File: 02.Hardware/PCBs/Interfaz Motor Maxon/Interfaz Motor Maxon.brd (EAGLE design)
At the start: 44.3 x 40.8 mm, 4 parts, among them J1 1-84953-1, J2 52207-1133

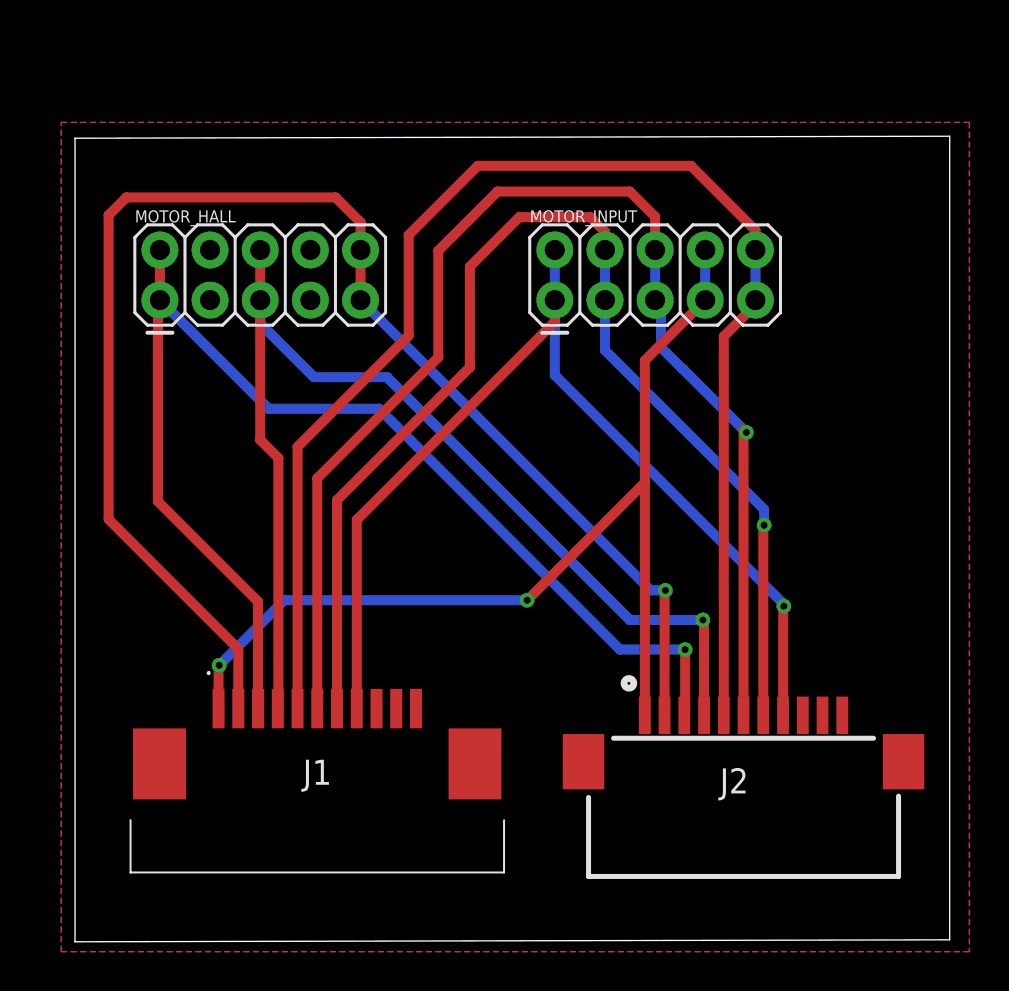
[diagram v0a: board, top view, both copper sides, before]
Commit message: añadidas vias entre planos masa top y bottom
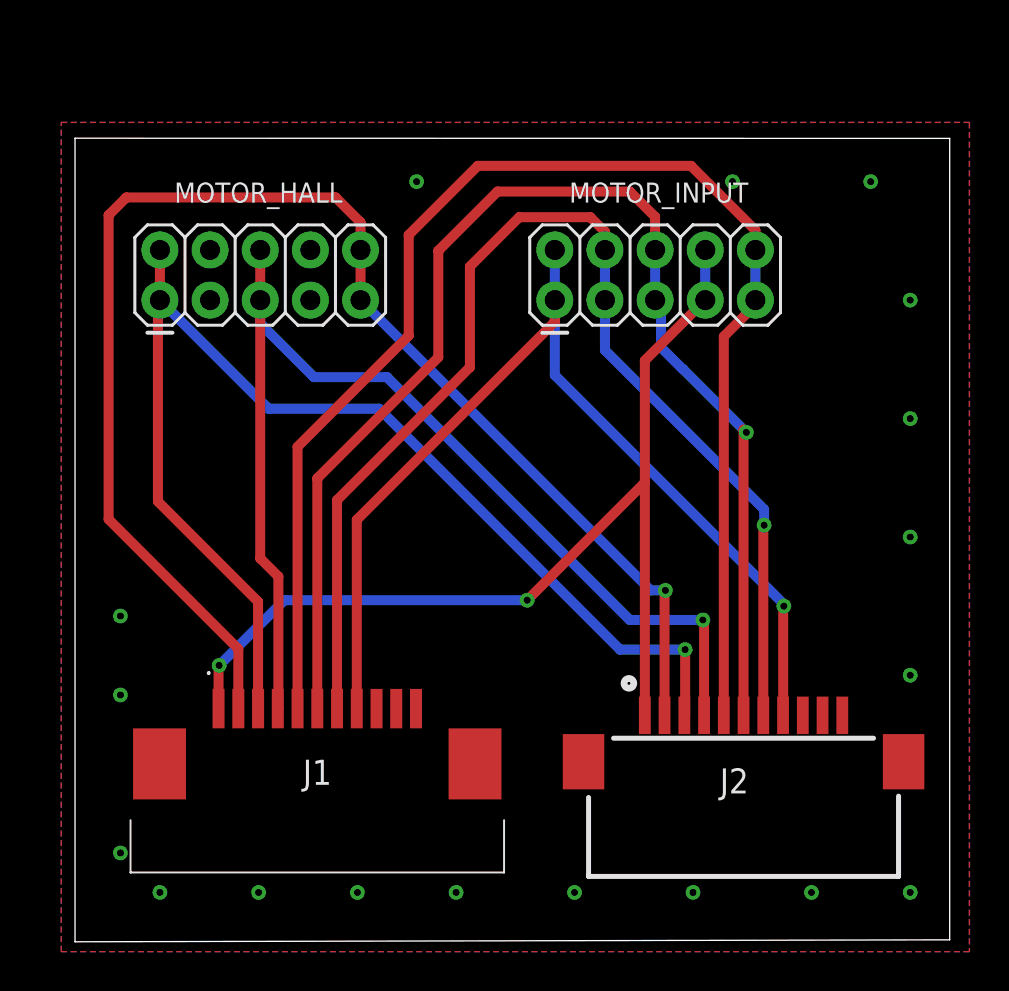
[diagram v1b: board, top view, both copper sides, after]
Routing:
- net GND: vias 0 -> 18
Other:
- board size 44.3 x 40.8 mm -> 44.3 x 40.7 mm
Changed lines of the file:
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@@
 <drawing>
 <settings>
-<setting alwaysvectorfont="no"/>
+<setting alwaysvectorfont="yes"/>
 <setting verticaltext="up"/>
 </settings>
@@
 <layer number="2" name="Route2" color="16" fill="1" visible="no" active="no"/>
 <layer number="15" name="Route15" color="23" fill="1" visible="no" active="no"/>
-<layer number="16" name="Bottom" color="1" fill="1" visible="yes" active="yes"/>
+<layer number="16" name="Bottom" color="1" fill="1" visible="no" active="yes"/>
 <layer number="17" name="Pads" color="2" fill="1" visible="yes" active="yes"/>
 <layer number="18" name="Vias" color="2" fill="1" visible="yes" active="yes"/>
@@
 <plain>
 <wire x1="1.7" y1="2.5" x2="46" y2="2.6" width="0" layer="20"/>
-<wire x1="46" y1="2.6" x2="46" y2="43.3" width="0" layer="20"/>
-<wire x1="46" y1="43.3" x2="1.7" y2="43.2" width="0" layer="20"/>
+<wire x1="46" y1="2.6" x2="46" y2="43.19" width="0" layer="20"/>
+<wire x1="46" y1="43.19" x2="1.7" y2="43.2" width="0" layer="20"/>
 <wire x1="1.7" y1="43.2" x2="1.7" y2="2.5" width="0" layer="20"/>
 <text x="42.8" y="22.9" size="1.778" layer="22" rot="MR0">Interfaz Maxon
@@
 </element>
 <element name="MOTOR_INPUT" library="SparkFun-Connectors" library_urn="urn:adsk.eagle:library:513" package="2X5" package3d_urn="urn:adsk.eagle:package:38012/1" value="" x="26" y="35" smashed="yes">
-<attribute name="NAME" x="24.73" y="38.937" size="0.6096" layer="25" font="vector" ratio="20"/>
+<attribute name="NAME" x="26.73" y="39.937" size="1.016" layer="25" font="vector" ratio="13"/>
 <attribute name="PROD_ID" value="CONN-08499" x="26" y="35" size="1.778" layer="27" display="off"/>
 <attribute name="SF_ID" value="PRT-0778" x="26" y="35" size="1.778" layer="27" display="off"/>
@@
 </element>
 <element name="MOTOR_HALL" library="SparkFun-Connectors" library_urn="urn:adsk.eagle:library:513" package="2X5" package3d_urn="urn:adsk.eagle:package:38012/1" value="" x="6" y="35" smashed="yes">
-<attribute name="NAME" x="4.73" y="38.937" size="0.6096" layer="25" font="vector" ratio="20"/>
+<attribute name="NAME" x="6.73" y="39.937" size="1.016" layer="25" font="vector" ratio="13"/>
 <attribute name="PROD_ID" value="CONN-08499" x="6" y="35" size="1.778" layer="27" display="off"/>
 <attribute name="SF_ID" value="PRT-0778" x="6" y="35" size="1.778" layer="27" display="off"/>
@@
 <contactref element="MOTOR_HALL" pad="5"/>
 <contactref element="MOTOR_HALL" pad="6"/>
-<wire x1="11.08" y1="35" x2="11.08" y2="34.7" width="0.508" layer="1"/>
-<wire x1="11.08" y1="34.7" x2="11.08" y2="27.92" width="0.508" layer="1"/>
-<wire x1="11.08" y1="27.92" x2="12" y2="27" width="0.508" layer="1"/>
-<wire x1="12" y1="27" x2="12" y2="14.34" width="0.508" layer="1"/>
+<wire x1="11.08" y1="35" x2="11.08" y2="21.92" width="0.508" layer="1"/>
+<wire x1="11.08" y1="21.92" x2="12" y2="21" width="0.508" layer="1"/>
+<wire x1="12" y1="21" x2="12" y2="14.34" width="0.508" layer="1"/>
 <wire x1="12" y1="14.34" x2="11.97" y2="14.31" width="0.508" layer="1"/>
 <wire x1="33.56" y1="13.97" x2="33.56" y2="18.74" width="0.508" layer="1"/>
@@
 <vertex x="1" y="2"/>
 </polygon>
+<via x="4" y="19" extent="1-16" drill="0.35"/>
+<via x="4" y="15" extent="1-16" drill="0.35"/>
+<via x="4" y="7" extent="1-16" drill="0.35"/>
+<via x="6" y="5" extent="1-16" drill="0.35"/>
+<via x="11" y="5" extent="1-16" drill="0.35"/>
+<via x="16" y="5" extent="1-16" drill="0.35"/>
+<via x="21" y="5" extent="1-16" drill="0.35"/>
+<via x="27" y="5" extent="1-16" drill="0.35"/>
+<via x="33" y="5" extent="1-16" drill="0.35"/>
+<via x="39" y="5" extent="1-16" drill="0.35"/>
+<via x="44" y="5" extent="1-16" drill="0.35"/>
+<via x="44" y="16" extent="1-16" drill="0.35"/>
+<via x="44" y="23" extent="1-16" drill="0.35"/>
+<via x="44" y="29" extent="1-16" drill="0.35"/>
+<via x="44" y="35" extent="1-16" drill="0.35"/>
+<via x="42" y="41" extent="1-16" drill="0.35"/>
+<via x="35" y="41" extent="1-16" drill="0.35"/>
+<via x="19" y="41" extent="1-16" drill="0.35"/>
 </signal>
 <signal name="MOTOR_C">

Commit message: Correcion errores. Interfaz Maxon v2
Correcion de conexiones entre los conectores del motores y los conectores a la placa.
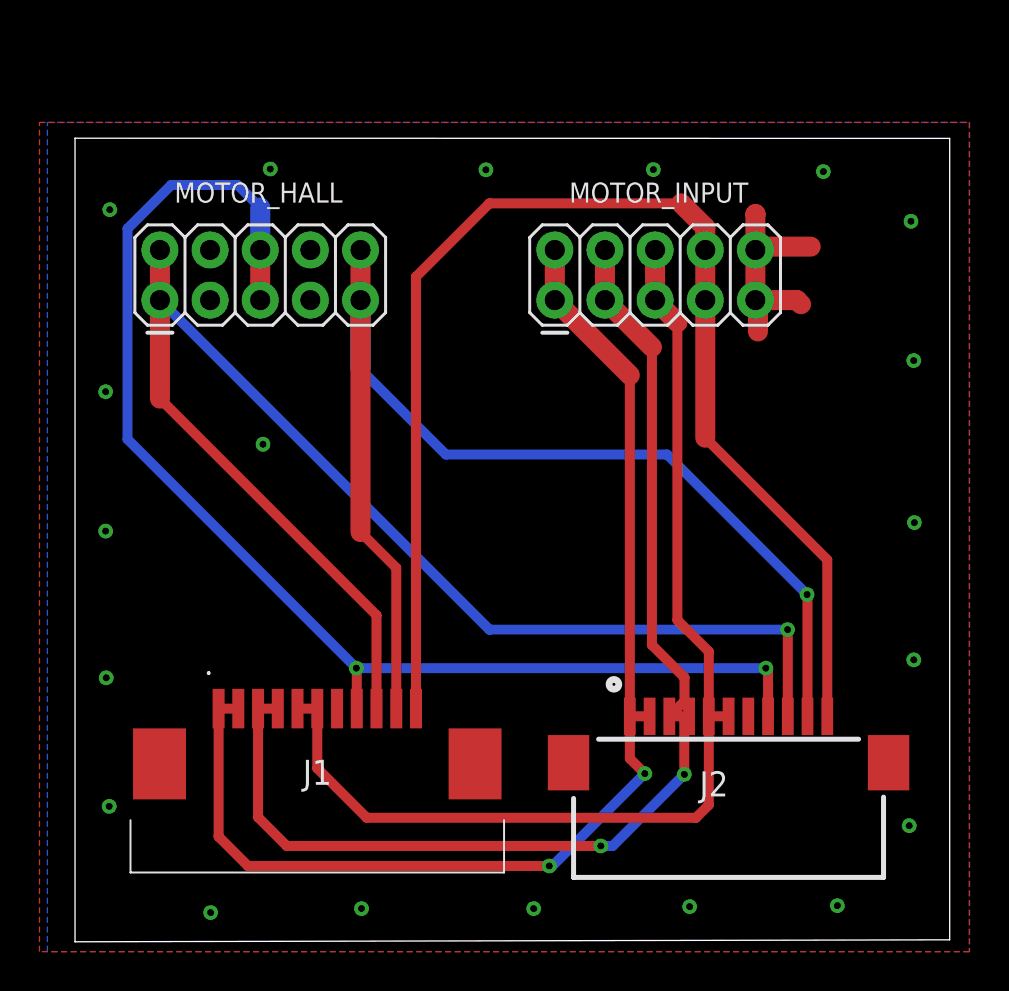
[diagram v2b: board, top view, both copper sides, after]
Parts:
- moved J2 0.76 mm to (34.8, 13.9)
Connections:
- net GND: now also J1.7, J2.7; no longer J1.5, J2.5
- net HALL_A: now also J1.9, J2.9; no longer J1.3, J2.3
- net HALL_B: now also J1.8, J2.8; no longer J1.4, J2.4
- net HALL_C: now also J1.10, J2.10; no longer J1.2, J2.2
- net MOTOR_A: now also J1.1, J1.2, J2.1, J2.2; no longer J1.8, J2.8
- net MOTOR_B: now also J1.3, J1.4, J2.3, J2.4; no longer J1.7, J2.7
- net MOTOR_C: now also J1.5, J2.5
- net VBUSBAR: now also J1.11, J2.11; no longer J1.1, J2.1
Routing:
- net GND: track 71.9 -> 11.3 mm, vias 18 -> 20
- net VBUSBAR: track 52.4 -> 65.9 mm, vias 2 -> 0
- net HALL_C: track 73.2 -> 61.0 mm
- net MOTOR_C: track 66.0 -> 55.4 mm, vias 1 -> 0
- net HALL_A: track 62.6 -> 70.9 mm
- net MOTOR_A: track 53.2 -> 61.0 mm, vias 1 -> 2
- net HALL_B: track 58.3 -> 65.1 mm, vias 1 -> 2
- net MOTOR_B: track 61.2 -> 59.9 mm, vias 1 -> 2
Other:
- board text added: "Interfaz Maxon v2-Oct22"
- board text removed: "Interfaz Maxon v1-Sep22"

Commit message: Adapatacion de la interfaz para conexión por trought hole directamente.
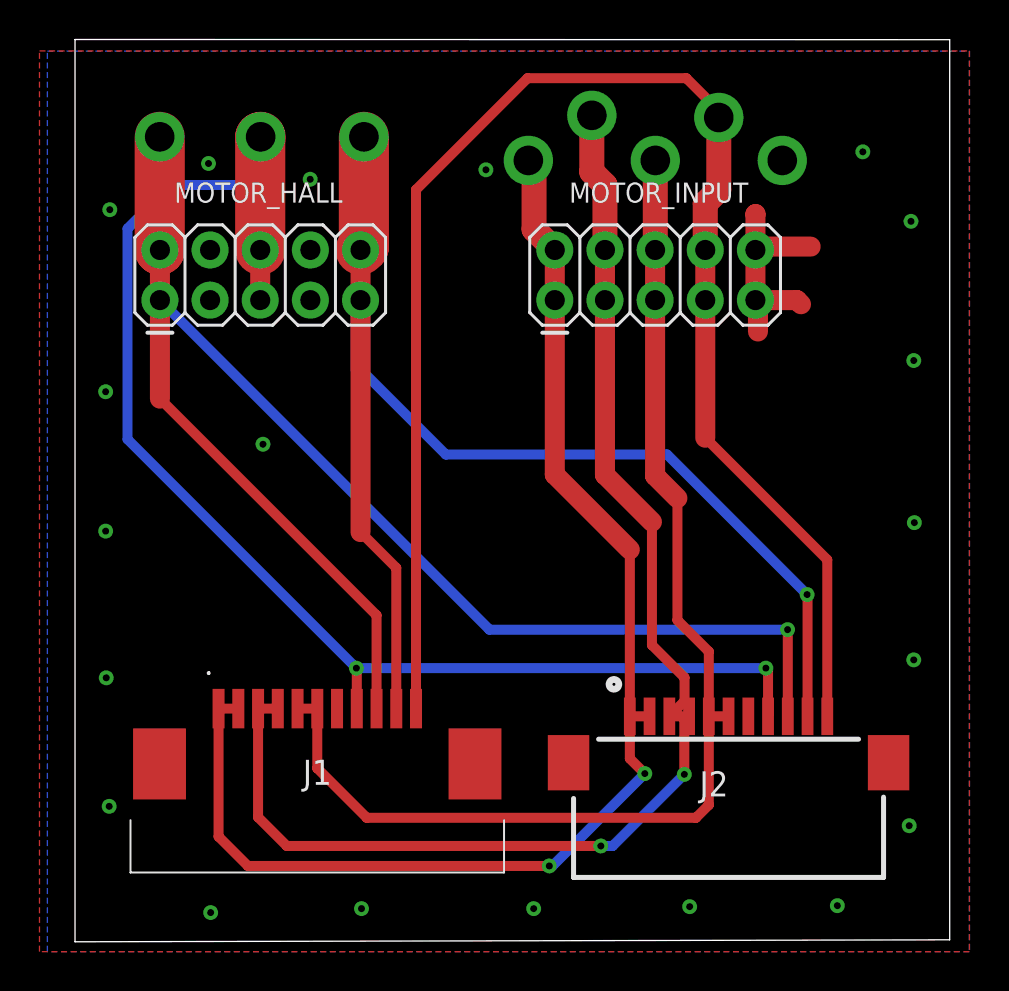
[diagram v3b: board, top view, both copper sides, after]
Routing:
- net VBUSBAR: track 65.9 -> 77.8 mm, vias 0 -> 1
- net MOTOR_B: track 59.9 -> 67.0 mm, vias 2 -> 3
- net HALL_C: track 61.0 -> 66.8 mm, vias 1 -> 2
- net HALL_B: track 65.1 -> 70.9 mm, vias 2 -> 3
- net HALL_A: track 70.9 -> 76.6 mm, vias 1 -> 2
- net MOTOR_A: track 61.0 -> 66.1 mm, vias 2 -> 3
- net MOTOR_C: track 55.4 -> 59.9 mm, vias 0 -> 1
- net GND: vias 20 -> 21
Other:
- board size 44.3 x 40.7 mm -> 44.3 x 45.7 mm
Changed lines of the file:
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@@
 <drawing>
 <settings>
-<setting alwaysvectorfont="yes"/>
+<setting alwaysvectorfont="no"/>
 <setting verticaltext="up"/>
 </settings>
@@
 <plain>
 <wire x1="1.7" y1="2.5" x2="46" y2="2.6" width="0" layer="20"/>
-<wire x1="46" y1="2.6" x2="46" y2="43.19" width="0" layer="20"/>
-<wire x1="46" y1="43.19" x2="1.7" y2="43.2" width="0" layer="20"/>
-<wire x1="1.7" y1="43.2" x2="1.7" y2="2.5" width="0" layer="20"/>
+<wire x1="46" y1="2.6" x2="46" y2="48.19" width="0" layer="20"/>
+<wire x1="46" y1="48.19" x2="1.7" y2="48.2" width="0" layer="20"/>
+<wire x1="1.7" y1="48.2" x2="1.7" y2="2.5" width="0" layer="20"/>
 <text x="42.8" y="22.9" size="1.778" layer="22" rot="MR0">Interfaz Maxon
 v2-Oct22</text>
@@
 <wire x1="20.48" y1="27.18" x2="16.16" y2="31.5" width="0.508" layer="16"/>
 <wire x1="16.16" y1="31.5" x2="16.16" y2="35" width="1.016" layer="16"/>
+<via x="16.33" y="43.27" extent="1-16" drill="1.5" diameter="2.5"/>
+<wire x1="16.33" y1="43.27" x2="16.33" y2="37.71" width="2.54" layer="1"/>
+<wire x1="16.33" y1="37.71" x2="16.16" y2="37.54" width="2.54" layer="1"/>
 </signal>
 <signal name="HALL_A">
@@
 <wire x1="37.79" y1="18.31" x2="22.69" y2="18.31" width="0.508" layer="16"/>
 <wire x1="22.69" y1="18.31" x2="6" y2="35" width="0.508" layer="16"/>
+<via x="5.99" y="43.27" extent="1-16" drill="1.5" diameter="2.5"/>
+<wire x1="5.99" y1="43.27" x2="5.99" y2="37.55" width="2.54" layer="1"/>
+<wire x1="5.99" y1="37.55" x2="6" y2="37.54" width="2.54" layer="1"/>
 </signal>
 <signal name="HALL_B">
@@
 <wire x1="9.94" y1="40.83" x2="11.08" y2="39.69" width="0.508" layer="16"/>
 <wire x1="11.08" y1="39.69" x2="11.08" y2="37.54" width="1.016" layer="16"/>
+<via x="11.1" y="43.27" extent="1-16" drill="1.5" diameter="2.5"/>
+<wire x1="11.08" y1="37.54" x2="11.08" y2="43.25" width="2.54" layer="1"/>
+<wire x1="11.08" y1="43.25" x2="11.1" y2="43.27" width="2.54" layer="1"/>
 </signal>
 <signal name="GND">
@@
 <contactref element="MOTOR_INPUT" pad="10"/>
 <polygon width="0.1524" layer="1">
-<vertex x="-0.1" y="44"/>
-<vertex x="47" y="44"/>
+<vertex x="-0.1" y="47.62"/>
+<vertex x="47" y="47.62"/>
 <vertex x="47" y="2"/>
 <vertex x="-0.1" y="2"/>
 </polygon>
 <polygon width="0.1524" layer="16">
-<vertex x="0.3" y="44"/>
-<vertex x="47" y="44"/>
+<vertex x="0.3" y="47.61"/>
+<vertex x="47" y="47.61"/>
 <vertex x="47" y="2"/>
 <vertex x="0.3" y="2"/>
@@
 <via x="44.18" y="31.94" extent="1-16" drill="0.35"/>
 <via x="44.04" y="38.99" extent="1-16" drill="0.35"/>
-<via x="39.6" y="41.51" extent="1-16" drill="0.35"/>
-<via x="30.99" y="41.61" extent="1-16" drill="0.35"/>
+<via x="41.6" y="42.51" extent="1-16" drill="0.35"/>
+<via x="8.46" y="41.92" extent="1-16" drill="0.35"/>
 <via x="22.51" y="41.6" extent="1-16" drill="0.35"/>
-<via x="11.59" y="41.64" extent="1-16" drill="0.35"/>
+<via x="13.61" y="41.12" extent="1-16" drill="0.35"/>
 <via x="11.22" y="27.7" extent="1-16" drill="0.35"/>
 <wire x1="36.16" y1="35" x2="38.26" y2="35" width="1.016" layer="1"/>
@@
 <wire x1="36.16" y1="37.54" x2="36.33" y2="37.71" width="1.016" layer="1"/>
 <wire x1="36.33" y1="37.71" x2="38.96" y2="37.71" width="1.016" layer="1"/>
+<via x="37.52" y="42.075" extent="1-16" drill="1.5" diameter="2.5"/>
 </signal>
 <signal name="MOTOR_C">
@@
 <contactref element="J1" pad="6"/>
 <wire x1="31.08" y1="37.54" x2="31.08" y2="35" width="1.016" layer="1"/>
-<wire x1="31.08" y1="35" x2="32.21" y2="33.87" width="1.016" layer="1"/>
-<wire x1="32.21" y1="33.87" x2="32.21" y2="18.79" width="0.508" layer="1"/>
+<wire x1="31.08" y1="35" x2="31.08" y2="26.1" width="1.016" layer="1"/>
+<wire x1="32.21" y1="24.97" x2="31.08" y2="26.1" width="1.016" layer="1"/>
+<wire x1="32.21" y1="24.97" x2="32.21" y2="18.79" width="0.508" layer="1"/>
 <wire x1="33.8" y1="17.2" x2="33.8" y2="13.92" width="0.508" layer="1"/>
 <wire x1="32.21" y1="18.79" x2="33.8" y2="17.2" width="0.508" layer="1"/>
@@
 <wire x1="12.97" y1="14.31" x2="13.97" y2="14.31" width="0.508" layer="1"/>
 <wire x1="34.8" y1="13.92" x2="33.8" y2="13.92" width="0.508" layer="1"/>
+<via x="31.09" y="42.075" extent="1-16" drill="1.5" diameter="2.5"/>
+<wire x1="31.08" y1="37.54" x2="31.09" y2="37.55" width="1.27" layer="1"/>
+<wire x1="31.09" y1="42.075" x2="31.09" y2="37.55" width="1.27" layer="1"/>
 </signal>
 <signal name="MOTOR_B">
@@
 <wire x1="32.5688" y1="15.8814625" x2="32.5688" y2="14.6888" width="0.508" layer="1"/>
 <wire x1="31.8" y1="13.92" x2="32.5688" y2="14.6888" width="0.508" layer="1"/>
-<wire x1="30.92" y1="32.62" x2="30.92" y2="17.5302625" width="0.508" layer="1"/>
-<wire x1="30.92" y1="32.62" x2="28.54" y2="35" width="1.016" layer="1"/>
+<wire x1="30.92" y1="23.77" x2="30.92" y2="17.5302625" width="0.508" layer="1"/>
+<wire x1="30.92" y1="23.77" x2="28.54" y2="26.15" width="1.016" layer="1"/>
+<wire x1="28.54" y1="26.15" x2="28.54" y2="35" width="1.016" layer="1"/>
 <wire x1="32.5688" y1="15.8814625" x2="30.92" y2="17.5302625" width="0.508" layer="1"/>
 <wire x1="10.97" y1="14.31" x2="11.97" y2="14.31" width="0.508" layer="1"/>
@@
 <wire x1="10.97" y1="8.81" x2="12.427" y2="7.353" width="0.508" layer="1"/>
 <wire x1="31.8" y1="13.92" x2="32.8" y2="13.92" width="0.508" layer="1"/>
+<via x="27.875" y="44.36" extent="1-16" drill="1.5" diameter="2.5"/>
+<wire x1="27.875" y1="44.36" x2="27.875" y2="41.495" width="1.27" layer="1"/>
+<wire x1="27.875" y1="41.495" x2="28.54" y2="40.83" width="1.27" layer="1"/>
+<wire x1="28.54" y1="40.83" x2="28.54" y2="37.54" width="1.27" layer="1"/>
 </signal>
 <signal name="MOTOR_A">
@@
 <contactref element="J2" pad="2"/>
 <wire x1="26" y1="37.54" x2="26" y2="35" width="1.016" layer="1"/>
-<wire x1="29.8" y1="31.2" x2="26" y2="35" width="1.016" layer="1"/>
-<wire x1="29.8" y1="31.2" x2="29.8" y2="13.92" width="0.508" layer="1"/>
+<wire x1="29.8" y1="22.36" x2="26" y2="26.16" width="1.016" layer="1"/>
+<wire x1="26" y1="26.16" x2="26" y2="35" width="1.016" layer="1"/>
+<wire x1="29.8" y1="22.36" x2="29.8" y2="13.92" width="0.508" layer="1"/>
 <wire x1="30.8" y1="13.92" x2="29.8" y2="13.92" width="0.508" layer="1"/>
 <wire x1="8.97" y1="14.31" x2="9.97" y2="14.31" width="0.508" layer="1"/>
@@
 <wire x1="8.97" y1="7.83" x2="10.46" y2="6.34" width="0.508" layer="1"/>
 <wire x1="10.46" y1="6.34" x2="25.72" y2="6.34" width="0.508" layer="1"/>
+<via x="24.66" y="42.075" extent="1-16" drill="1.5" diameter="2.5"/>
+<wire x1="24.95" y1="41.785" x2="24.95" y2="38.59" width="1.27" layer="1"/>
+<wire x1="26" y1="37.54" x2="24.95" y2="38.59" width="1.27" layer="1"/>
+<wire x1="24.66" y1="42.075" x2="24.95" y2="41.785" width="1.27" layer="1"/>
 </signal>
 <signal name="VBUSBAR">
@@
 <wire x1="33.62" y1="28.03" x2="39.8" y2="21.85" width="0.508" layer="1"/>
 <contactref element="J1" pad="11"/>
-<wire x1="22.69" y1="39.9" x2="18.97" y2="36.18" width="0.508" layer="1"/>
-<wire x1="18.97" y1="14.31" x2="18.97" y2="36.18" width="0.508" layer="1"/>
-<wire x1="22.69" y1="39.9" x2="32.4" y2="39.9" width="0.508" layer="1"/>
-<wire x1="32.4" y1="39.9" x2="33.62" y2="38.68" width="1.016" layer="1"/>
-<wire x1="33.62" y1="38.68" x2="33.62" y2="37.54" width="1.016" layer="1"/>
+<wire x1="24.62" y1="46.24" x2="18.97" y2="40.59" width="0.508" layer="1"/>
+<wire x1="18.97" y1="14.31" x2="18.97" y2="40.59" width="0.508" layer="1"/>
+<wire x1="24.62" y1="46.24" x2="32.66" y2="46.24" width="0.508" layer="1"/>
+<wire x1="32.66" y1="46.24" x2="34.33" y2="44.57" width="0.508" layer="1"/>
+<wire x1="33.62" y1="39.9" x2="33.62" y2="37.54" width="1.27" layer="1"/>
+<via x="34.305" y="44.25" extent="1-16" drill="1.5" diameter="2.5"/>
+<wire x1="34.305" y1="44.25" x2="34.305" y2="40.585" width="1.27" layer="1"/>
+<wire x1="34.305" y1="40.585" x2="33.62" y2="39.9" width="1.27" layer="1"/>
+<wire x1="34.33" y1="44.57" x2="34.305" y2="44.25" width="0" layer="19" extent="1-1"/>
 </signal>
 </signals>
